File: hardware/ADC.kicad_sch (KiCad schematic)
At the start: 22 parts, among them U12 ADS7128

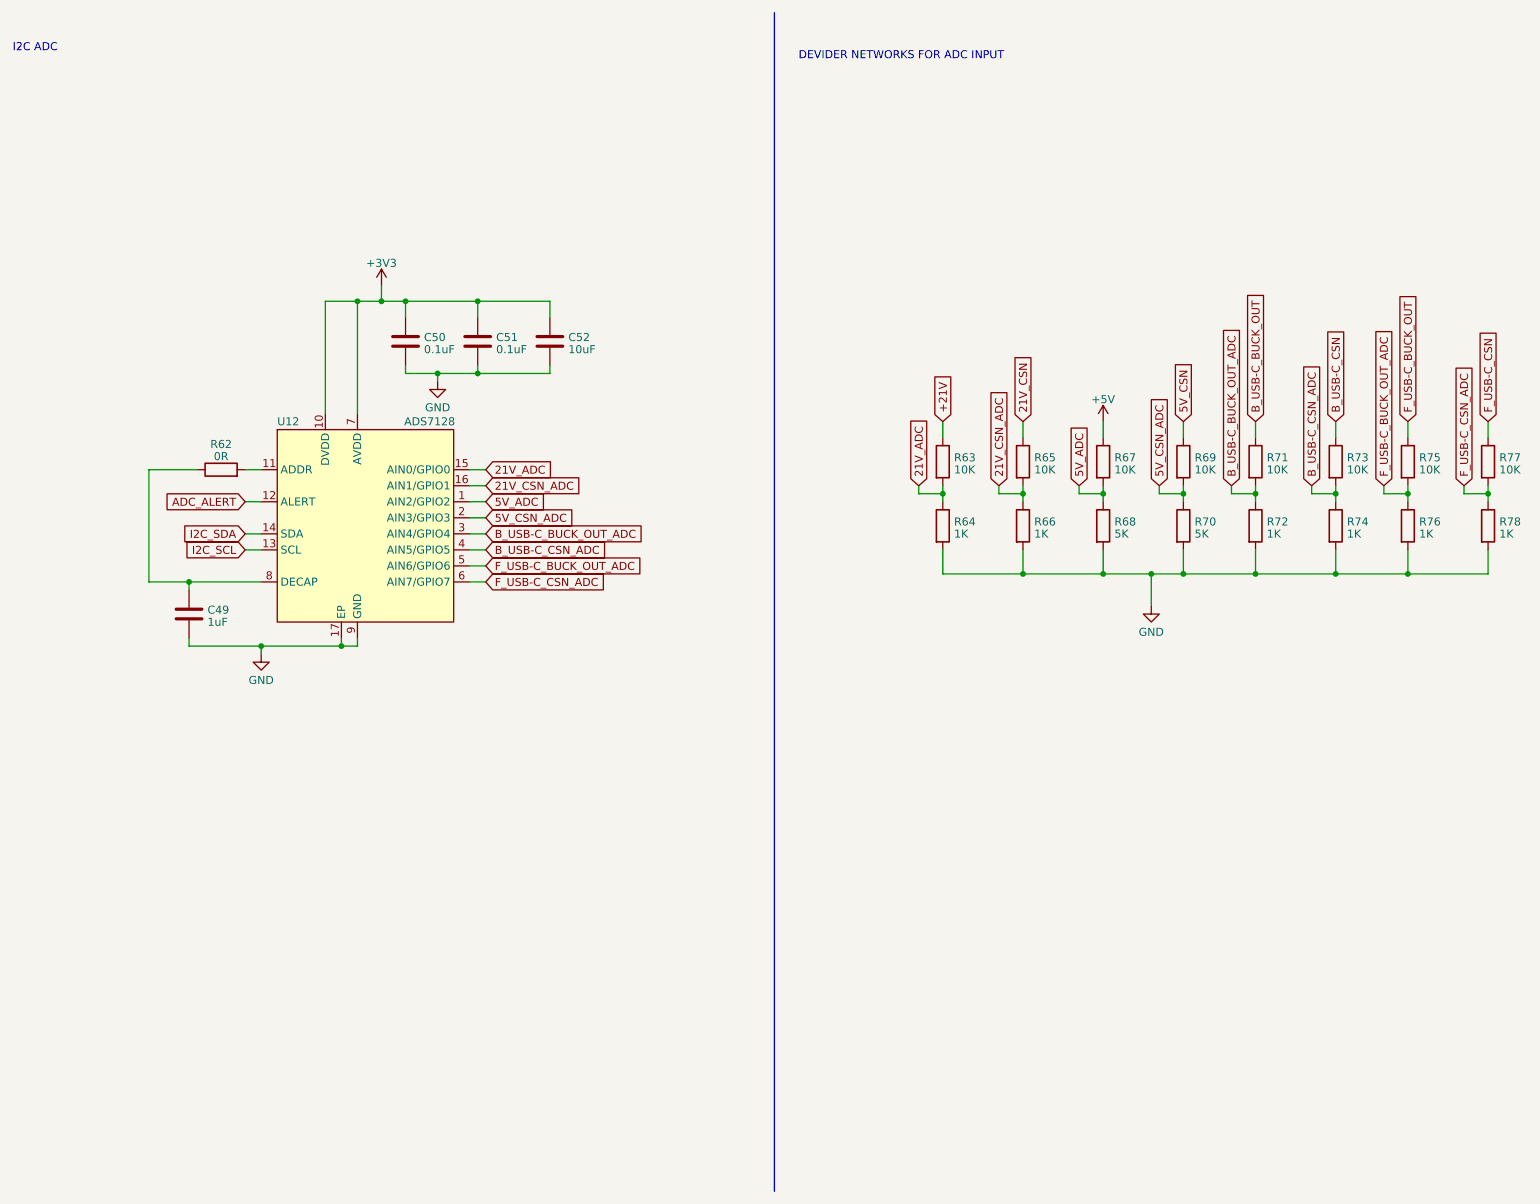
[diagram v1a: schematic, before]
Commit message: migrated to the esp32-s2 and starting new board revison
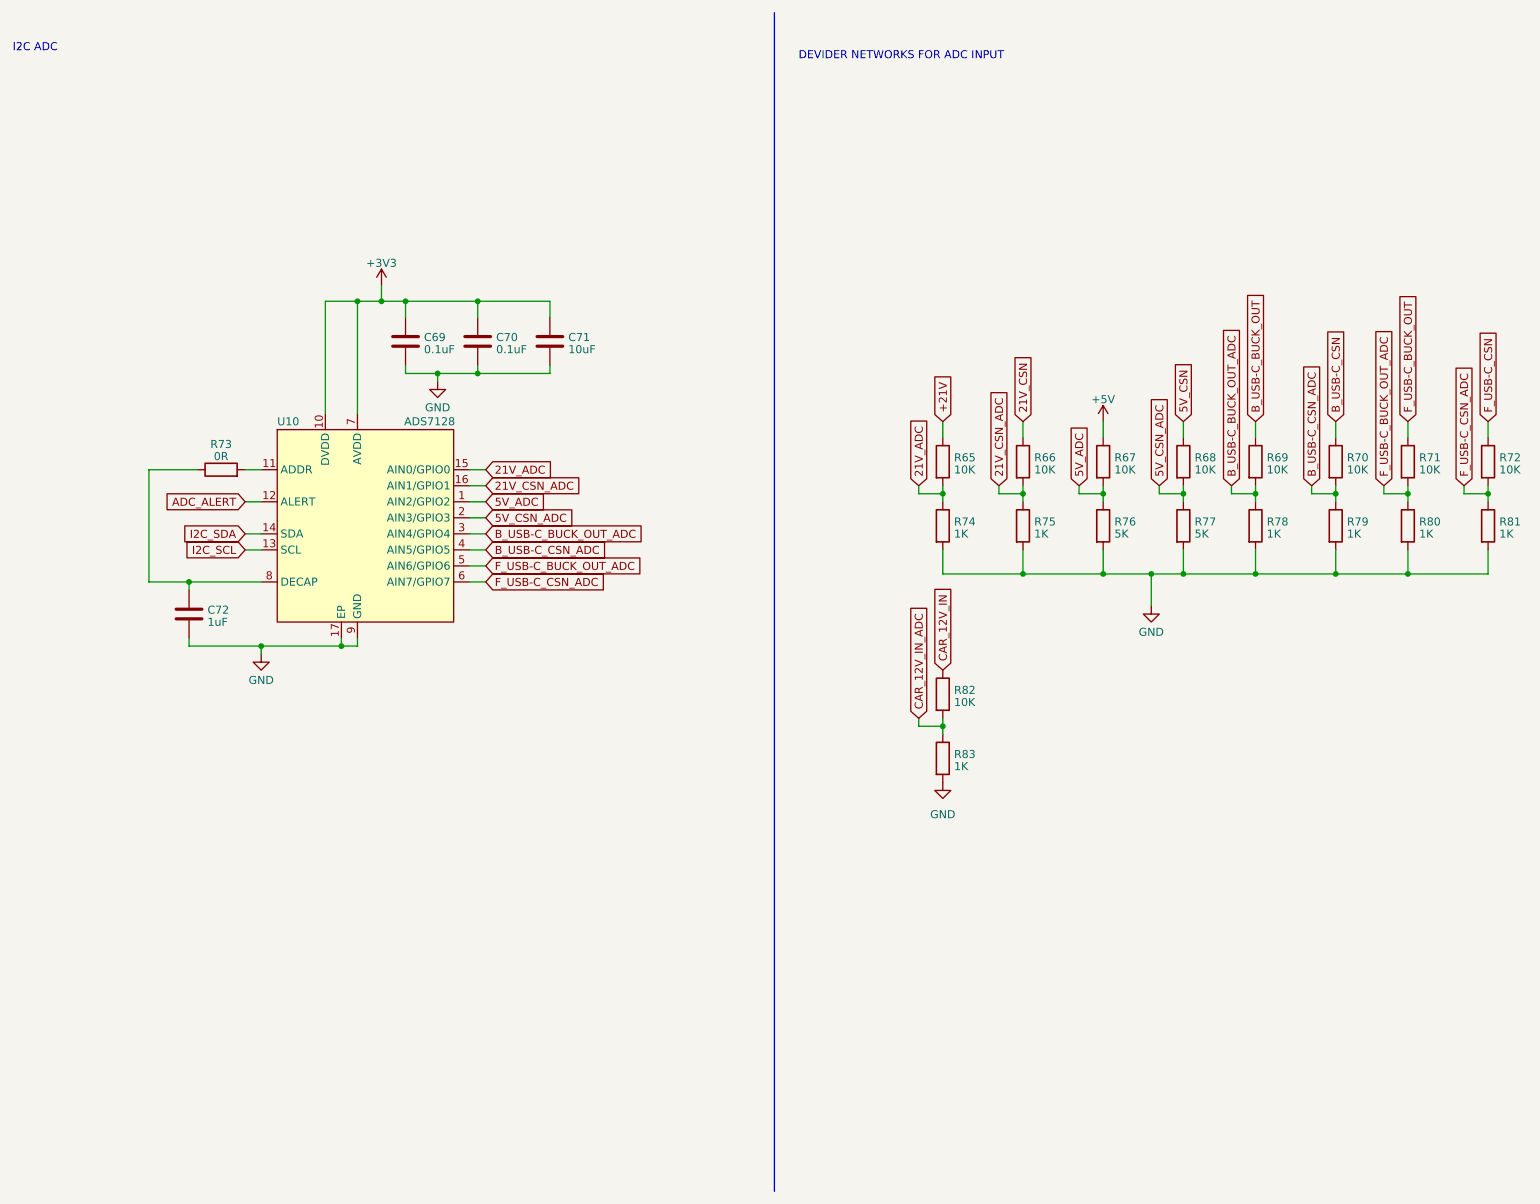
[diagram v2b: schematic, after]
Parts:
- added R82: 10K, Resistor_SMD:R_0603_1608Metric, symbol Device:R
- added R83: 1K, Resistor_SMD:R_0603_1608Metric, symbol Device:R
- U10: renamed from U12; value ADS7128 -> ADS7128
- renumbered C50 to C69, C51 to C70, C52 to C71, C49 to C72, R63 to R65, R65 to R66, R69 to R68, R71 to R69, R73 to R70, R75 to R71, R77 to R72, R62 to R73, R64 to R74, R66 to R75, R68 to R76, R70 to R77, R72 to R78, R74 to R79, R76 to R80, R78 to R81
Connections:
- net GND: now also R83.2
- new net CAR_12V_IN: R82.1
- new net CAR_12V_IN_ADC: R82.2, R83.1
